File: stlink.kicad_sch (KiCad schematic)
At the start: 36 parts, among them Con4 USB_C_Wurth_632723130112, Q1 BC847B, U5 STM32F103C(8-B)Tx, U6 MCP1700T-3302E_MB, X1 8.000MHZ

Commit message: Reworked schematic and applied changes on pcb related with mini pci express
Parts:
- C22, C23, C24, C25, C28, C29: symbol Capacitors_Smd0603:100nF_0603 -> Capacitors_Smd0603:100n
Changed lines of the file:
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@@
     (pin "2")
   )
-  (symbol (lib_id "Capacitors_Smd0603:100nF_0603") (at 93.98 90.17 0) (unit 1)
+  (symbol (lib_id "Capacitors_Smd0603:100n") (at 93.98 90.17 0) (unit 1)
     (in_bom yes) (on_board yes)
     (property "Reference" "C28" (id 0) (at 97.3074 89.0016 0)
@@
     (pin "2")
   )
-  (symbol (lib_id "Capacitors_Smd0603:100nF_0603") (at 114.3 193.04 0) (unit 1)
+  (symbol (lib_id "Capacitors_Smd0603:100n") (at 114.3 193.04 0) (unit 1)
     (in_bom yes) (on_board yes)
     (property "Reference" "C22" (id 0) (at 117.6274 191.8716 0)
@@
     (pin "2")
   )
-  (symbol (lib_id "Capacitors_Smd0603:100nF_0603") (at 125.73 90.17 0) (unit 1)
+  (symbol (lib_id "Capacitors_Smd0603:100n") (at 125.73 90.17 0) (unit 1)
     (in_bom yes) (on_board yes)
     (property "Reference" "C29" (id 0) (at 129.0574 89.0016 0)
@@
     (pin "2")
   )
-  (symbol (lib_id "Capacitors_Smd0603:100nF_0603") (at 127 193.04 0) (unit 1)
+  (symbol (lib_id "Capacitors_Smd0603:100n") (at 127 193.04 0) (unit 1)
     (in_bom yes) (on_board yes)
     (property "Reference" "C23" (id 0) (at 130.3274 191.8716 0)
@@
     (pin "2")
   )
-  (symbol (lib_id "Capacitors_Smd0603:100nF_0603") (at 139.7 193.04 0) (unit 1)
+  (symbol (lib_id "Capacitors_Smd0603:100n") (at 139.7 193.04 0) (unit 1)
     (in_bom yes) (on_board yes)
     (property "Reference" "C24" (id 0) (at 143.0274 191.8716 0)
@@
     (pin "2")
   )
-  (symbol (lib_id "Capacitors_Smd0603:100nF_0603") (at 152.4 193.04 0) (unit 1)
+  (symbol (lib_id "Capacitors_Smd0603:100n") (at 152.4 193.04 0) (unit 1)
     (in_bom yes) (on_board yes)
     (property "Reference" "C25" (id 0) (at 155.7274 191.8716 0)

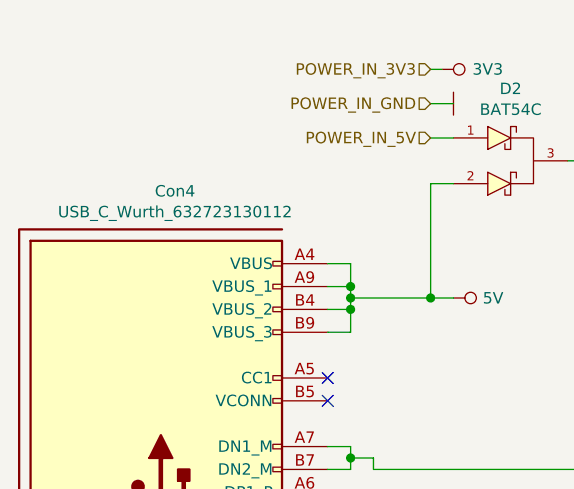
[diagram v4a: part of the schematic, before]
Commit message: Aligned USB C connectors on schematic and on pcb
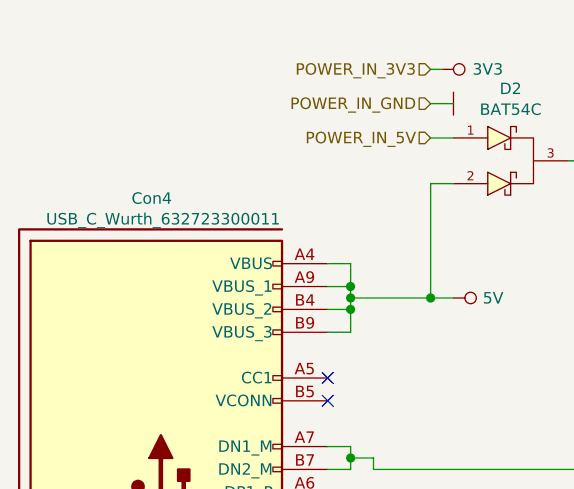
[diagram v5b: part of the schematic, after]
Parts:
- removed Con4: USB_C_Wurth_632723130112, Connector_USB:USB_C_632723130112, symbol USB_Connectors:USB_C_Wurth_632723130112
- added Con4: USB_C_Wurth_632723300011, Connector_USB:632723300011, symbol USB_Connectors:USB_C_Wurth_632723300011
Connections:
- net 5V: now also Con4.A4 (VBUS), Con4.A9 (VBUS_1), Con4.B4 (VBUS_2), Con4.B9 (VBUS_3)
- net GND: now also Con4.A1 (GND), Con4.A12 (GND_1), Con4.B1 (GND_2), Con4.B12 (GND_3)
- net at R13.1, R15.2: now also Con4.A6 (DP1_P), Con4.B6 (DP2_P)
- net at R12.2: now also Con4.A7 (DN1_M), Con4.B7 (DN2_M)
- net at C26.2: now also Con4.S1 (SHIELD), Con4.S2 (SHIELD), Con4.S3 (SHIELD), Con4.S4 (SHIELD)
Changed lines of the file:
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@@
     (pin "3")
   )
-  (symbol (lib_id "USB_Connectors:USB_C_Wurth_632723130112") (at 44.45 127 0) (unit 1)
+  (symbol (lib_id "USB_Connectors:USB_C_Wurth_632723300011") (at 44.45 127 0) (unit 1)
     (in_bom yes) (on_board yes)
-    (property "Reference" "Con4" (id 0) (at 46.5328 85.9282 0))
-    (property "Value" "USB_C_Wurth_632723130112" (id 1) (at 46.5328 88.2396 0))
-    (property "Footprint" "Connector_USB:USB_C_632723130112" (id 2) (at 45.72 124.46 0)
+    (property "Reference" "Con4" (id 0) (at 43.942 86.7368 0))
+    (property "Value" "USB_C_Wurth_632723300011" (id 1) (at 45.212 89.0355 0))
+    (property "Footprint" "Connector_USB:632723300011" (id 2) (at 45.72 124.46 0)
       (effects (font (size 1.27 1.27)) hide)
     )
-    (property "Datasheet" "https://www.we-online.com/catalog/datasheet/632723130112.pdf" (id 3) (at 45.72 124.46 0)
+    (property "Datasheet" "https://pl.mouser.com/datasheet/2/445/632723300011-1718173.pdf" (id 3) (at 45.72 124.46 0)
       (effects (font (size 1.27 1.27)) hide)
     )
@@
       (effects (font (size 1.27 1.27)) hide)
     )
-    (property "Manufacturer Part Number" "632723130112" (id 5) (at 45.72 127 0)
+    (property "Manufacturer Part Number" "632723300011" (id 5) (at 45.72 127 0)
       (effects (font (size 1.27 1.27)) hide)
     )
@@
       (effects (font (size 1.27 1.27)) hide)
     )
-    (property "Supplier Part Number" "710-632723130112" (id 7) (at 45.72 127 0)
+    (property "Supplier Part Number" "710-632723300011" (id 7) (at 45.72 127 0)
       (effects (font (size 1.27 1.27)) hide)
     )
-    (property "URL" "https://pl.mouser.com/ProductDetail/Wurth-Elektronik/632723130112?qs=2WXlatMagcEknienHxbwUw%3D%3D" (id 8) (at 45.72 127 0)
+    (property "URL" "https://pl.mouser.com/ProductDetail/Wurth-Elektronik/632723300011?qs=NK6InXoXhq4%252B5eM1PePLPg%3D%3D" (id 8) (at 45.72 127 0)
       (effects (font (size 1.27 1.27)) hide)
     )
-    (property "Price@1pc" "21,34" (id 9) (at 45.72 127 0)
+    (property "Price@1pc" "17,55" (id 9) (at 45.72 127 0)
       (effects (font (size 1.27 1.27)) hide)
     )
-    (property "Price@1000pcs" "13,16" (id 10) (at 45.72 127 0)
+    (property "Price@1000pcs" "11,70" (id 10) (at 45.72 127 0)
       (effects (font (size 1.27 1.27)) hide)
     )

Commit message: Updated schematic
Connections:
- net STM-JTMS-~RESET~ renamed STM-JTMS-~{RESET}
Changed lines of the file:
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@@
-(kicad_sch (version 20210406) (generator eeschema)
+(kicad_sch (version 20210615) (generator eeschema)
   (paper "A3")
   (title_block
@@
     (effects (font (size 1.27 1.27)) (justify right))
   )
-  (hierarchical_label "STM-JTMS-~RESET~" (shape input) (at 83.82 177.8 180)
+  (hierarchical_label "STM-JTMS-~{RESET}" (shape input) (at 83.82 177.8 180)
     (effects (font (size 1.27 1.27)) (justify right))
   )
